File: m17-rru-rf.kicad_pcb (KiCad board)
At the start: 4 copper layers, 202 x 125 mm, 224 parts, among them J1 LMT87LPM, J2 13.8V, J3 N_PAD, J4 DBG_CONN, J5 SWD_CONN, J6 DA15_CONN, J7 N_PAD, Q1 BSS138, Q2 BSS138, Q3 NP100P04PDG, U1 LT1013DIDR, U10 GAT-30+, U11 CC1200, U12 AD8318, U13 AD8318, U14 STM32F405RGT6, U15 WH3538X-1, U2 LM317_SOT-223, U3 TL431, U4 RA60H3847H1, U5 TP6841, U6 TP6841, U7 CC1200, U8 GAT-30+, U9 SYBD-30-62HP+, X1 40MHz, Y1 12MHz

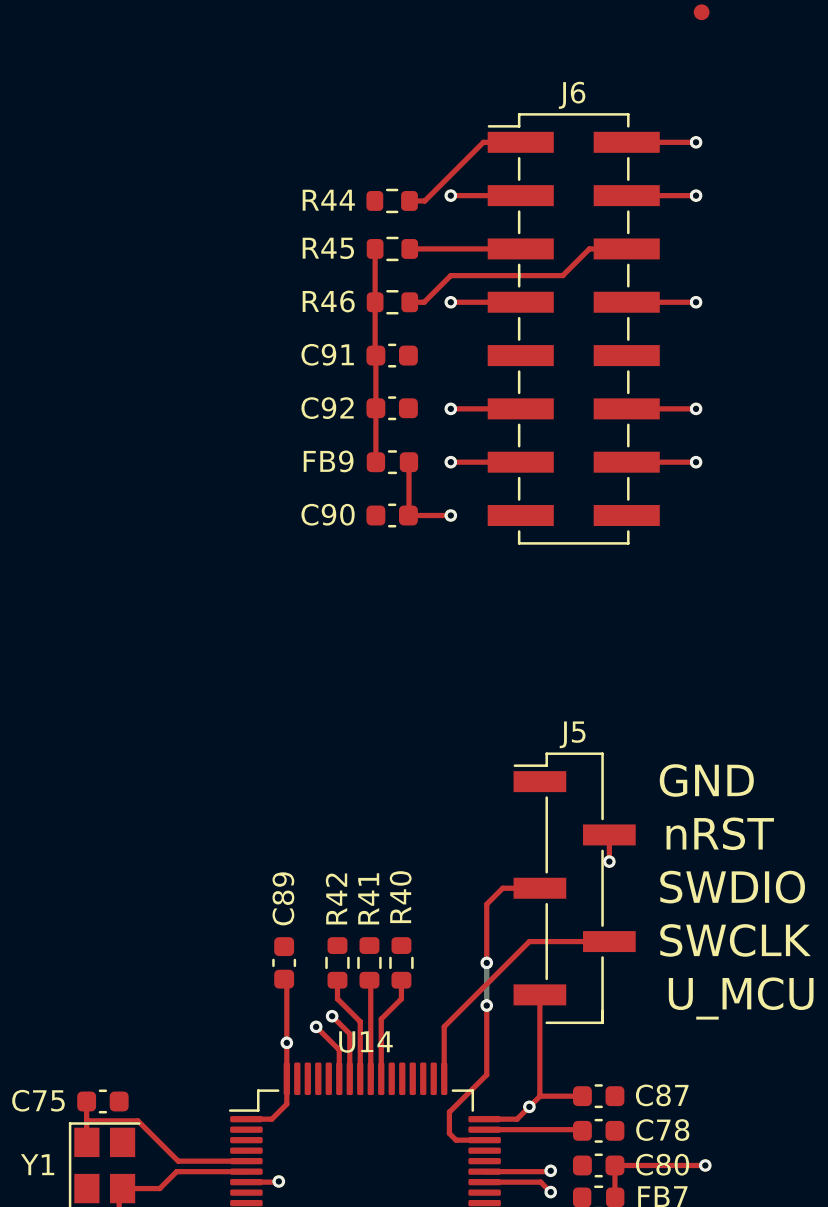
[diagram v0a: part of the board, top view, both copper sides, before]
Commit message: `DA15_CONN` pinout change
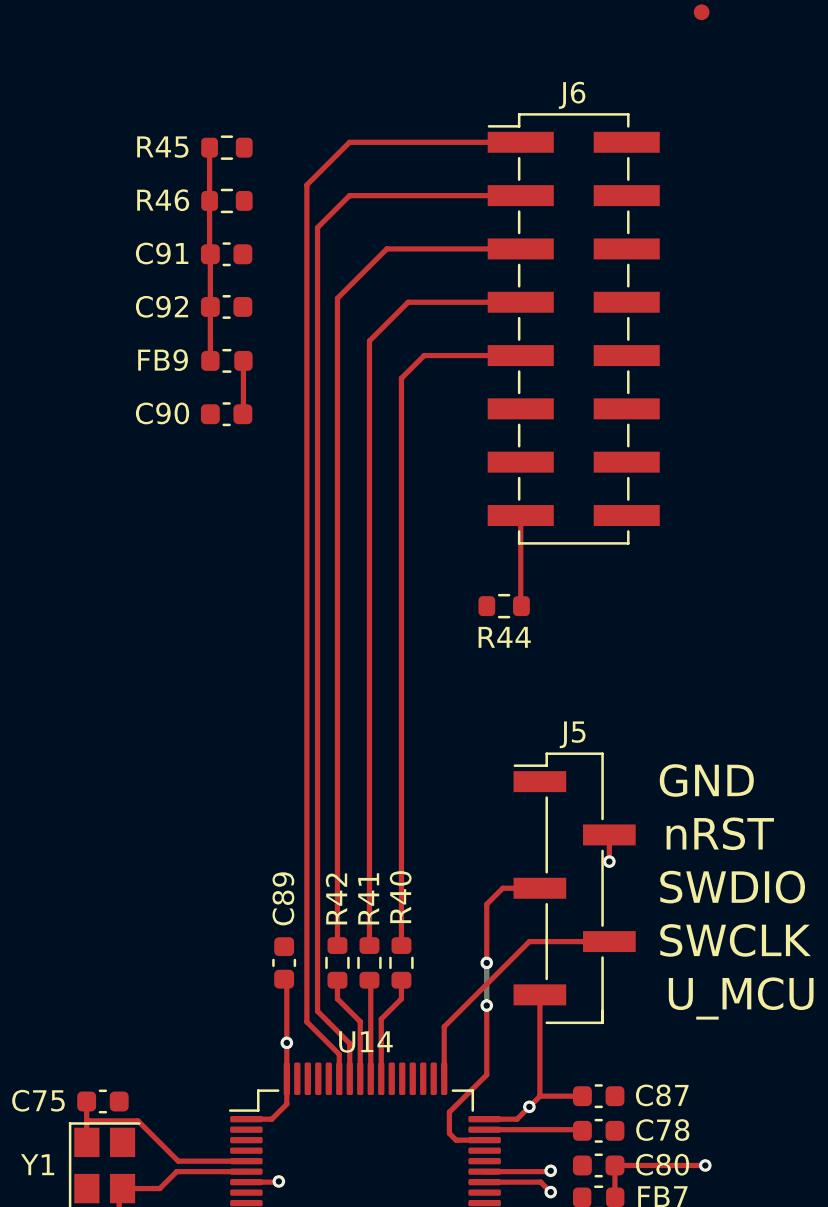
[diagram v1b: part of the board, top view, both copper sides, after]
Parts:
- moved R44 20.0 mm to (148.6, 82.3)
- moved C91 9.25 mm to (135.4, 65.5)
- moved FB9 9.25 mm to (135.4, 70.6)
- moved R45 9.25 mm to (135.4, 60.5)
- moved R46 9.25 mm to (135.4, 63.0)
- moved C90 9.25 mm to (135.4, 73.2)
- moved C92 9.25 mm to (135.4, 68.0)
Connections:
- J6 pad 1: /nRST -> /TX_nCS
- J6 pad 10: GND -> /Interface/MCU_TX
- J6 pad 12: /Interface/TEMP_SENSE -> /Interface/MCU_RX
- J6 pad 13: /FWD_SENSE -> GND
- J6 pad 14: /REF_SENSE -> /FWD_SENSE
- J6 pad 15: GND -> /nRST
- J6 pad 16: GND -> /REF_SENSE
- J6 pad 2: /SPI_MISO -> GND
- J6 pad 3: /SPI_MOSI -> /RX_nCS
- J6 pad 4: /SPI_SCK -> GND
- J6 pad 5: /TX_nCS -> /SPI_MOSI
- J6 pad 6: /RX_nCS -> GND
- J6 pad 7: /Interface/MCU_TX -> /SPI_MISO
- J6 pad 8: /Interface/MCU_RX -> /Interface/TEMP_SENSE
- J6 pad 9: GND -> /SPI_SCK
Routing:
- net /TX_nCS: track 13.9 -> 60.2 mm, vias 2 -> 1
- net /SPI_MOSI: track 39.2 -> 76.4 mm, vias 3 -> 2
- net /RX_nCS: track 24.4 -> 61.2 mm, vias 3 -> 2
- net /SPI_MISO: track 31.5 -> 65.0 mm, vias 4 -> 3
- net /SPI_SCK: track 34.7 -> 64.6 mm, vias 3 -> 2
- net /Exciter/3.3V_IN: track 137.5 -> 117.1 mm, vias 6 -> 5
- net /Interface/MCU_TX: track 6.68 -> 3.35 mm, vias 2 -> 1
- net /Interface/PA_EN: track 3.33 -> 0.00 mm, vias 1 -> 0
- net /FWD_SENSE: track 46.6 -> 43.3 mm, vias 4 -> 3
- net /REF_SENSE: track 11.6 -> 8.29 mm, vias 2 -> 1
- net /Interface/TEMP_SENSE: track 3.30 -> 0.00 mm, vias 1 -> 0
- net /Interface/MCU_RX: track 6.47 -> 3.17 mm, vias 2 -> 1
- net /nRST: track 74.5 -> 72.2 mm

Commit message: pcb routing update
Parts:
- moved H7 24.5 mm to (142.0, 134.5)
- moved C90 3.31 mm to (135.6, 69.8)
- moved R44 3.30 mm to (151.9, 82.3), turned to 0 degrees
- moved FID1 3.03 mm to (126.0, 159.3)
- moved FID3 2.34 mm to (311.9, 137.2)
- moved FB9 2.30 mm to (135.6, 68.3)
- moved R45 1.80 mm to (135.6, 62.2)
- moved C92 1.27 mm to (135.6, 66.8)
- moved TP9 0.94 mm to (224.0, 101.9)
- moved TP8 0.94 mm to (218.9, 101.9)
- moved R46 0.80 mm to (135.6, 63.8)
- moved C91 0.37 mm to (135.6, 65.3)
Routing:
- net /Power supply/5V_OUT: track 16.9 -> 255.2 mm, vias 1 -> 2
- net /Interface/PA_EN: track 0.00 -> 140.9 mm, vias 0 -> 2
- net /RX_nCS: track 61.2 -> 184.5 mm, vias 2 -> 5
- net /Interface/TEMP_SENSE: track 0.00 -> 122.8 mm, vias 0 -> 4
- net /Exciter/3.3V_IN: track 117.1 -> 239.0 mm, vias 5 -> 7
- net /MCU/PA_EN: track 0.00 -> 120.3 mm, vias 0 -> 3
- net /SPI_SCK: track 64.6 -> 167.1 mm, vias 2 -> 3
- net /SPI_MOSI: track 76.4 -> 177.1 mm, vias 2 -> 3
- net /nRST: track 72.2 -> 170.6 mm, vias 4 -> 3
- net /SPI_MISO: track 65.0 -> 161.0 mm, vias 3 -> 4
- net /Power supply/13.8V_OUT: track 208.9 -> 303.6 mm
- net /TX_nCS: track 60.2 -> 150.7 mm, vias 1 -> 4
- net /REF_SENSE: track 8.29 -> 77.4 mm, vias 1 -> 3
- net /FWD_SENSE: track 43.3 -> 101.1 mm, vias 3 -> 4
- net /Exciter/40M_OUT: track 13.3 -> 63.3 mm, vias 1 -> 2
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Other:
- board text added: "40MHz"
- board text added: "PA_VGG"
- board text added: "PWR_SP"

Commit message: silkscreen update
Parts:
- added REF**: OSHW-Logo_11.4x12mm_SilkScreen, Symbol:OSHW-Logo_11.4x12mm_SilkScreen, F.Cu at (235.0, 155.0)
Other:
- board text added: "ALC"
- board text added: "Exciter"
- board text added: "Isolator RF power sensing"
- board text added: "MCU"
- board text added: "PSU"
- board text added: "RF PA"
- board text added: "RF input filter"
- board text added: "Receiver"
- board text added: "Remote Radio Unit RF board Wojciech Kaczmarski, SP5WWP M17 Project, October 2023"

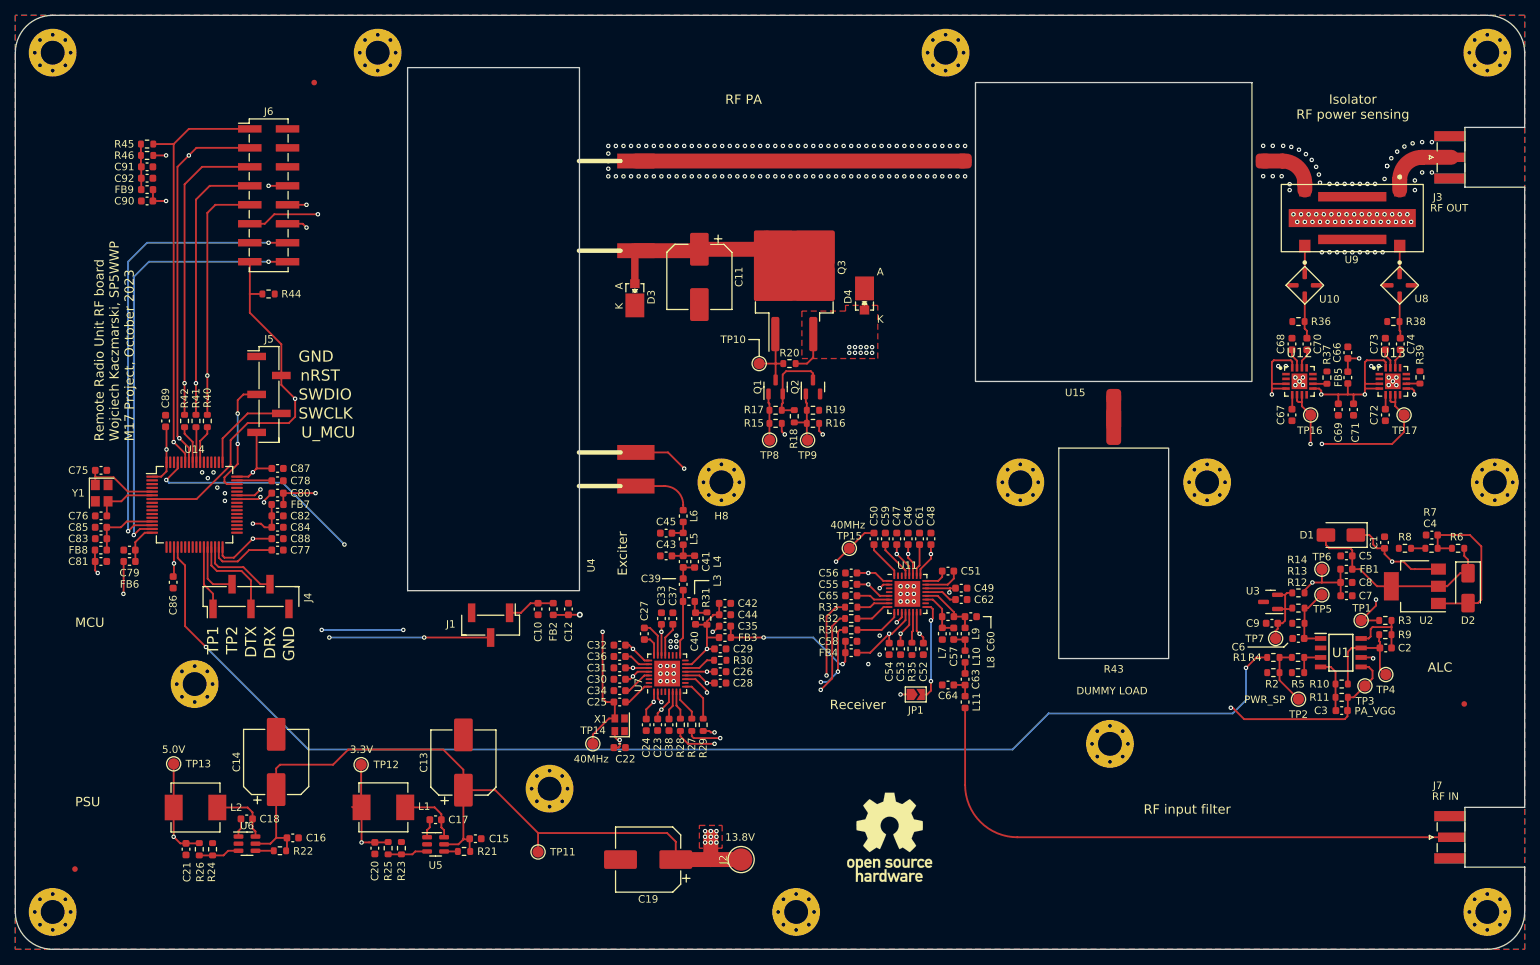
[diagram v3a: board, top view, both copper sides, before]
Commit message: some via fencing
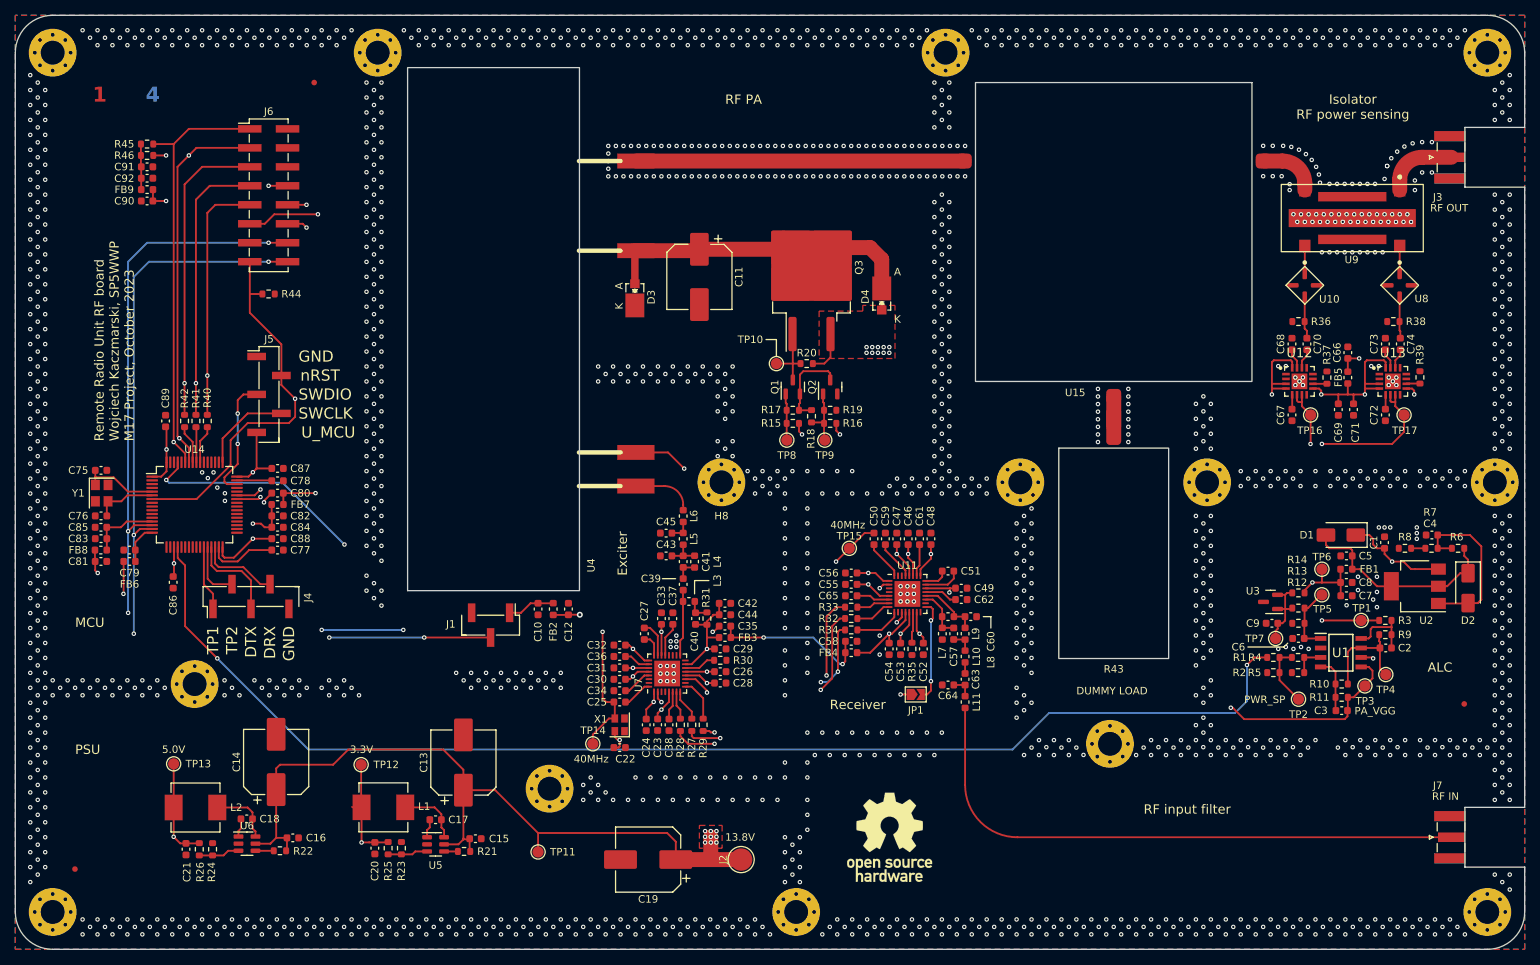
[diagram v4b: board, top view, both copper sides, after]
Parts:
- moved D4 2.31 mm to (234.0, 82.5)
- moved Q1 2.31 mm to (222.1, 94.7)
- moved Q2 2.31 mm to (227.1, 94.7)
- moved Q3 2.31 mm to (224.6, 80.0)
- moved R15 2.31 mm to (222.1, 99.6)
- moved R16 2.31 mm to (227.1, 99.6)
- moved R17 2.31 mm to (222.1, 97.9)
- moved R18 2.31 mm to (224.6, 98.7)
- moved R19 2.31 mm to (227.1, 97.9)
- moved R20 2.31 mm to (223.9, 91.6)
- moved TP10 2.31 mm to (219.9, 91.6)
- moved TP9 2.31 mm to (226.3, 101.9)
- moved TP8 2.30 mm to (221.3, 101.9)
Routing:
- net /REF_SENSE: track 77.4 -> 304.7 mm, vias 3 -> 4
- net /FWD_SENSE: track 101.1 -> 302.0 mm, vias 4 -> 5
- net /RF PA/RF_PA_VDD: track 28.5 -> 42.0 mm
- net /MCU/PA_EN: track 120.3 -> 122.6 mm
- net /Interface/PA_EN: track 140.9 -> 143.2 mm
- net /Interface/TEMP_SENSE: track 122.8 -> 121.1 mm
- net /Power supply/13.8V_OUT: track 303.6 -> 305.0 mm
- net /RX_nCS: track 184.5 -> 183.8 mm, vias 5 -> 4
- net /SPI_SCK: track 167.1 -> 166.4 mm
- net /SPI_MOSI: track 177.1 -> 176.4 mm
- net GND: vias 222 -> 1699
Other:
- board text added: "1"
- board text added: "2"
- board text added: "3"
- board text added: "3.2mm"
- board text added: "4"

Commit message: DRU fixes
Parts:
- renumbered REF** to #SYM1
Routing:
- net GND: track 2.85 -> 8.72 mm, vias 1699 -> 2121
- net /MCU/PA_EN: track 122.6 -> 123.8 mm
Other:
- outline, holes or cut-outs redrawn
- board text added: "Dummy load"
- board text removed: "DUMMY LOAD"

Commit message: update
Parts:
- moved J3 3.00 mm to (313.0, 64.0)
- moved J7 3.00 mm to (313.0, 155.0)
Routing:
- net /RF coupler/RF_OUT_CONN: track 9.91 -> 12.4 mm
- net /RF input filter/RF_OUT: track 79.1 -> 80.4 mm
- net GND: vias 2121 -> 2126
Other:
- outline, holes or cut-outs redrawn
